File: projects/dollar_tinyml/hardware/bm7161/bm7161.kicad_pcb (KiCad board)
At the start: 2 copper layers, 12 x 15.5 mm, 28 parts, among them P1 Header 1, P2 Header 4, Y1 32MHz/12pF

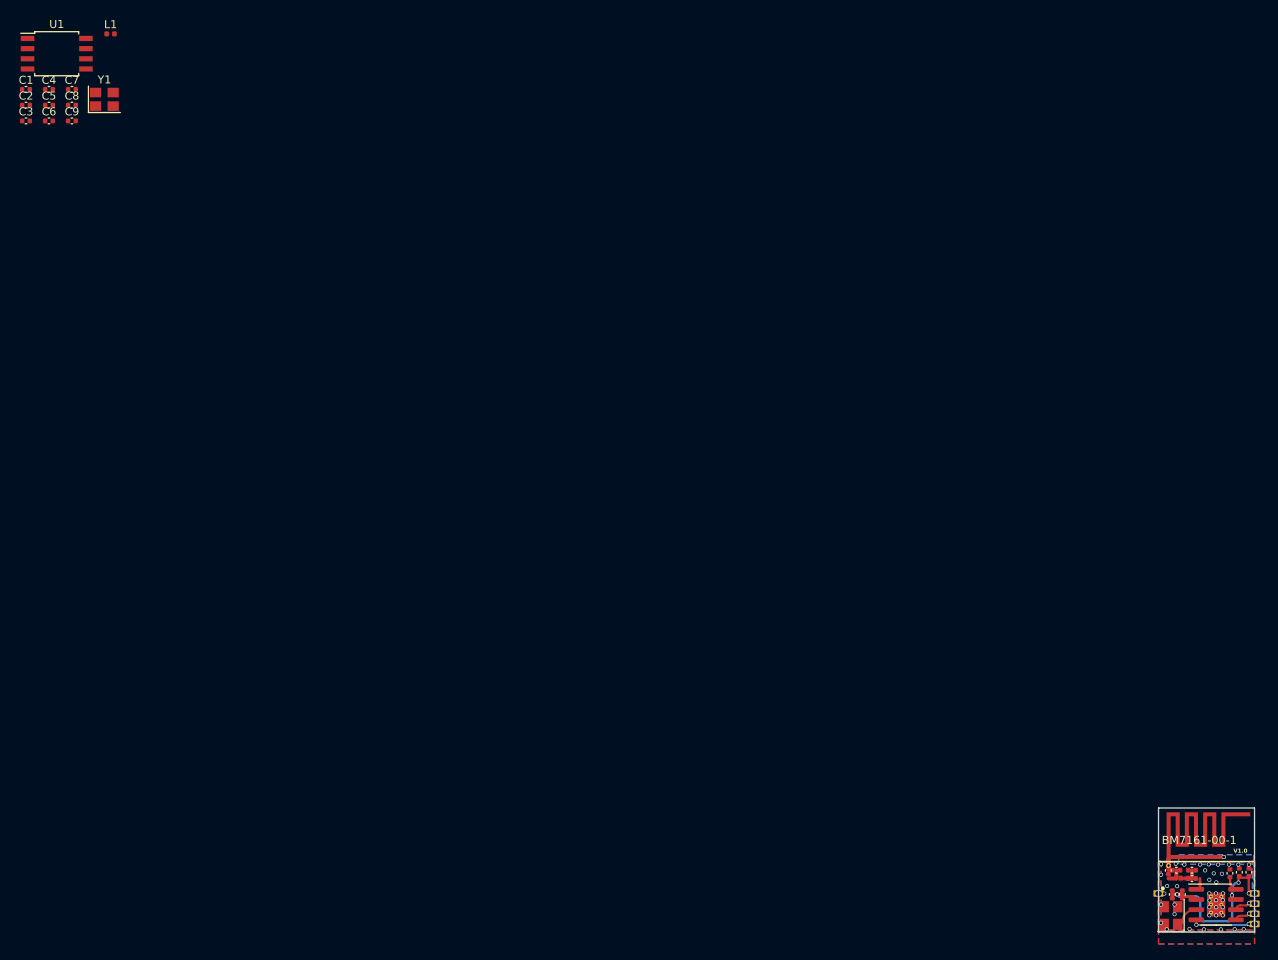
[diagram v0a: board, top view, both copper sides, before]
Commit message: dollarml: Use BM7161 3d model
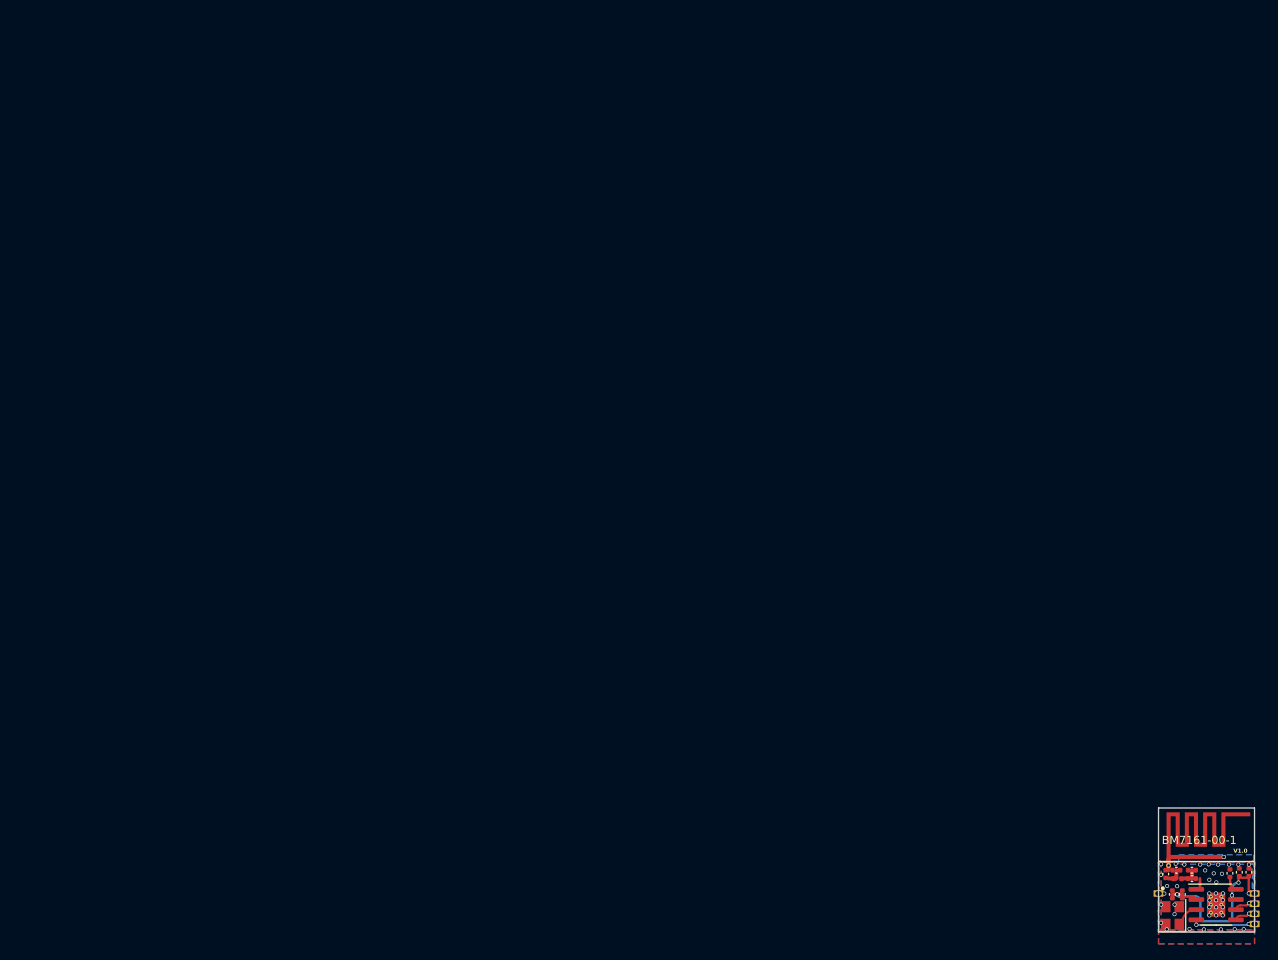
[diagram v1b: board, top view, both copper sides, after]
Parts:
- removed the C1 at (0.94, 7.43)
- removed the C2 at (0.94, 9.40)
- removed the C3 at (0.94, 11.4)
- removed the C4 at (3.81, 7.43)
- removed the C5 at (3.81, 9.40)
- removed the C6 at (3.81, 11.4)
- removed the C7 at (6.67, 7.43)
- removed the C8 at (6.67, 9.40)
- removed the C9 at (6.67, 11.4)
- removed the L1 at (11.5, 0.49)
- removed the U1 at (4.78, 2.98)
- removed the Y1 at (10.7, 8.68)
- moved L1 0.87 mm to (144.9, 106.1)
- moved C1 0.56 mm to (143.4, 105.5)
- moved Y1 0.20 mm to (144.3, 110.7)
